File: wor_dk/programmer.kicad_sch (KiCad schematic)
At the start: 44 parts, among them J501 Prog_Ext, J502 USB_C_Receptacle_USB2.0_14P, J503 Prog, Q501 BSS84, SW501 SW_Push, U501 TLV1117-33, U502 LPC11U35FHI33_501, Y501 Crystal

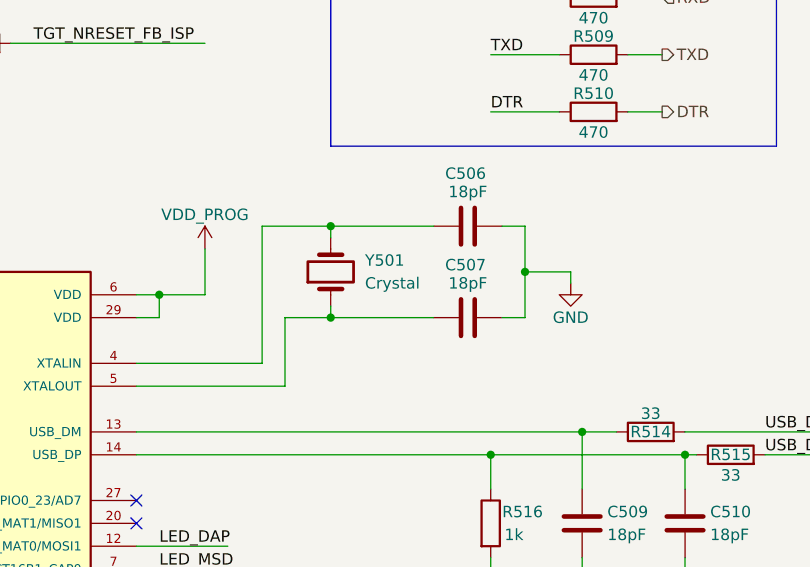
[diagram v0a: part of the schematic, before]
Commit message: wor_dk: add footprints & part info for transistor & ICs
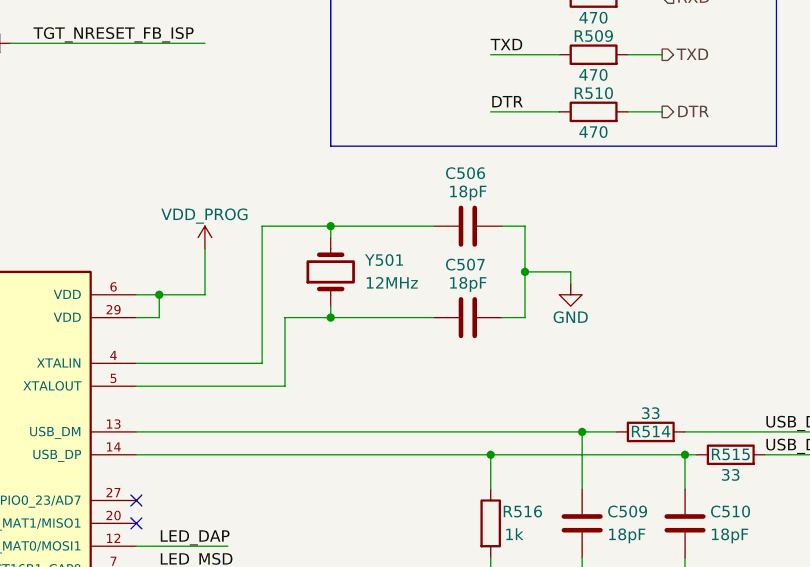
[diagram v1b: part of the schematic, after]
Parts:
- Q501: LCSC (none) -> C493579; MPN (none) -> BSS84,215; Manufacturer (none) -> Nexperia
- U501: footprint (none) -> Package_TO_SOT_SMD:SOT-223; LCSC (none) -> C37359; MPN (none) -> TLV1117-33IDCYR; Manufacturer (none) -> Texas Instruments
- Y501: value Crystal -> 12MHz
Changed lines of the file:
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@@
 			)
 		)
-		(property "Value" "Crystal"
+		(property "Value" "12MHz"
 			(at 224.79 88.8999 90)
 			(effects
@@
 			)
 		)
-		(property "Footprint" ""
+		(property "Footprint" "Package_TO_SOT_SMD:SOT-223"
 			(at 123.19 26.67 0)
 			(effects
@@
 			)
 		)
+		(property "LCSC" "C37359"
+			(at 123.19 26.67 0)
+			(effects
+				(font
+					(size 1.27 1.27)
+				)
+				(hide yes)
+			)
+		)
+		(property "MPN" "TLV1117-33IDCYR"
+			(at 123.19 26.67 0)
+			(effects
+				(font
+					(size 1.27 1.27)
+				)
+				(hide yes)
+			)
+		)
+		(property "Manufacturer" "Texas Instruments"
+			(at 123.19 26.67 0)
+			(effects
+				(font
+					(size 1.27 1.27)
+				)
+				(hide yes)
+			)
+		)
 		(pin "2"
 		)
@@
 			(at 236.22 125.73 0)
 			(effects
+				(font
+					(size 1.27 1.27)
+				)
+				(hide yes)
+			)
+		)
+		(property "LCSC" "C493579"
+			(at 236.22 125.73 0)
+			(effects
+				(font
+					(size 1.27 1.27)
+				)
+				(hide yes)
+			)
+		)
+		(property "MPN" "BSS84,215"
+			(at 236.22 125.73 0)
+			(effects
+				(font
+					(size 1.27 1.27)
+				)
+				(hide yes)
+			)
+		)
+		(property "Manufacturer" "Nexperia"
+			(at 236.22 125.73 0)
+			(effects

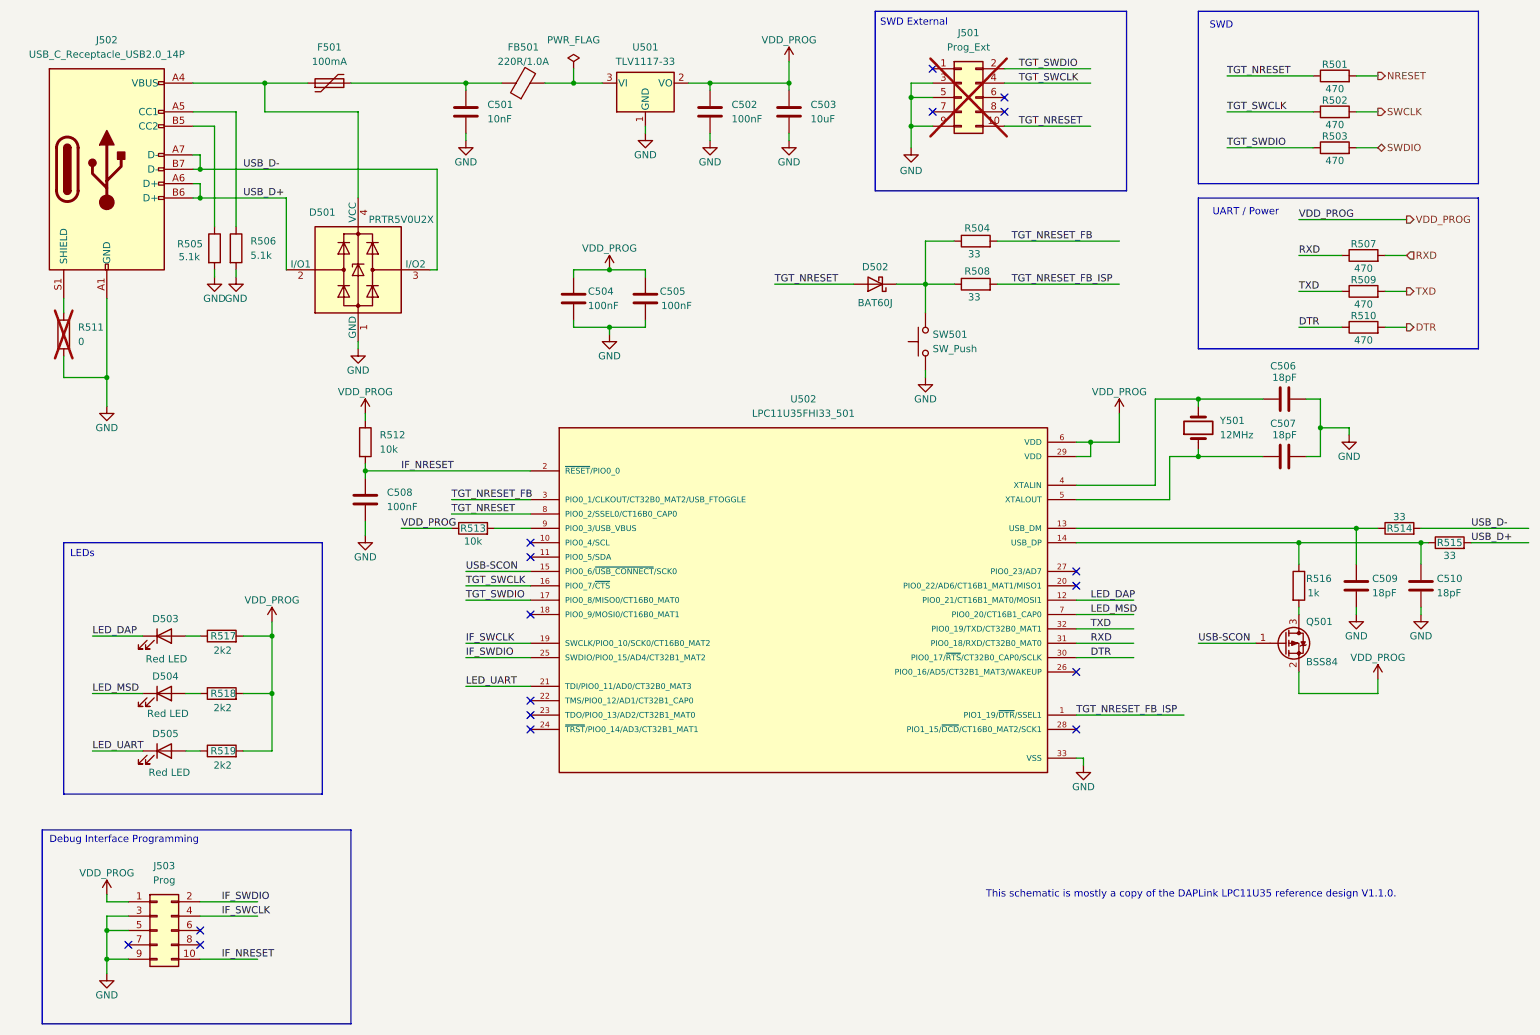
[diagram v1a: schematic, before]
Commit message: wor_dk: add all footprints & part info for connectors
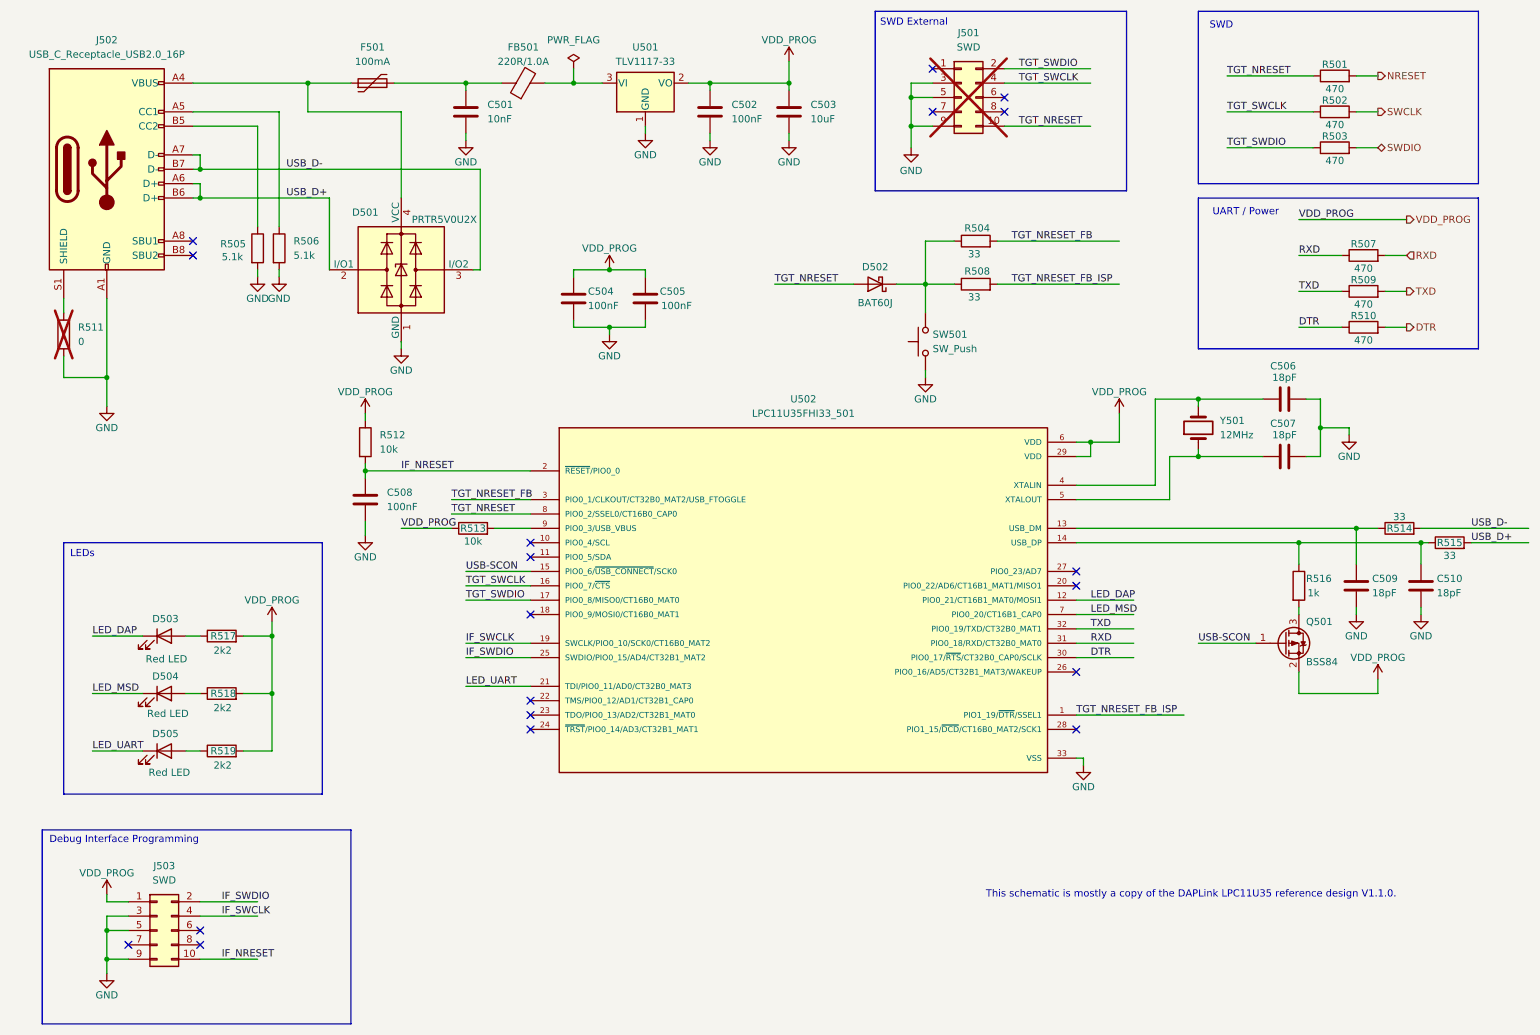
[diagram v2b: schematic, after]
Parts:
- removed J502: USB_C_Receptacle_USB2.0_14P, symbol Connector:USB_C_Receptacle_USB2.0_14P
- added J502: USB_C_Receptacle_USB2.0_16P, Connector_USB:USB_C_Receptacle_GCT_USB4105-xx-A_16P_TopMnt_Horizontal, symbol Connector:USB_C_Receptacle_USB2.0_16P
- J501: value Prog_Ext -> SWD; Comment (none) -> Connector for debugging / flashing external device; LCSC (none) -> C598540; MPN (none) -> 20021121-00010T4LF; Manufacturer (none) -> Amphenol ICC
- J503: value Prog -> SWD; Comment (none) -> Connector for debugging / flashing LCP11U35; LCSC (none) -> C598540; MPN (none) -> 20021121-00010T4LF; Manufacturer (none) -> Amphenol ICC
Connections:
- net GND: now also J502.A1 (GND), J502.A12 (GND), J502.B1 (GND), J502.B12 (GND)
- net USB_D+: now also J502.A6 (D+), J502.B6 (D+)
- net USB_D-: now also J502.A7 (D-), J502.B7 (D-)
- net at R505.1: now also J502.B5 (CC2)
- net at D501.4 (VCC), F501.1: now also J502.A4 (VBUS), J502.A9 (VBUS), J502.B4 (VBUS), J502.B9 (VBUS)
- net at R506.1: now also J502.A5 (CC1)
- net at R511.1: now also J502.S1 (SHIELD)
- no-connect marks 17 -> 19
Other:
- moved on the sheet: D501, F501, R505, R506

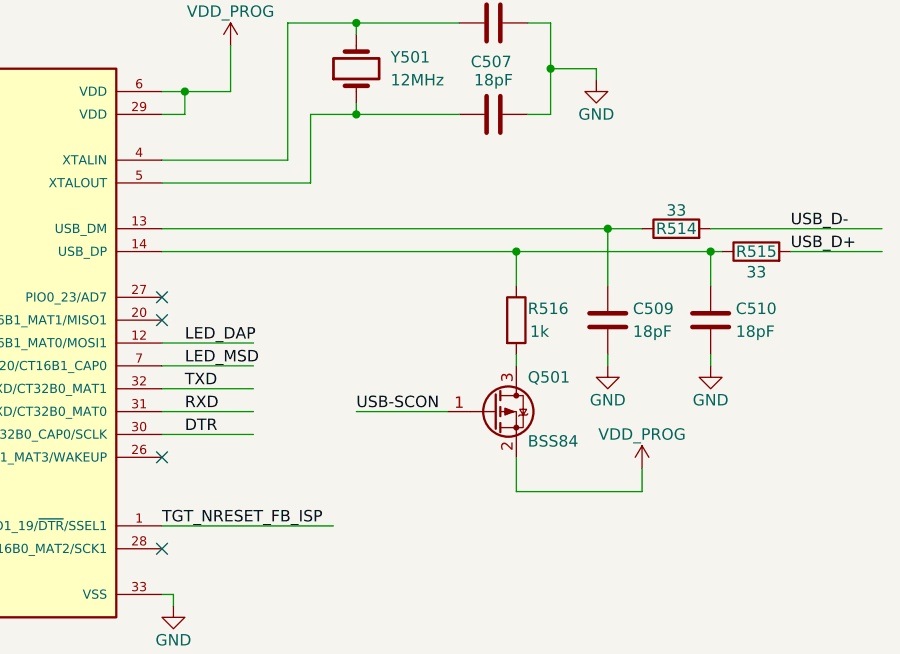
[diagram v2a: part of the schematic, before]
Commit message: wor_dk: add/modify USB data line filtering
- add filtering as suggested by FTDI application note AN232B-06
  section 6.2:
  "Some USB 2.0 hubs appear to be extremely sensitive to noise. A
  glitch on the USB lines can in some cases cause a device to hang.
  This problem can be fixed by adding two 47pF capacitors to ground on
  the USB DP and USB DM lines. These should be located between the 27W
  series resistors and the hub."
- using 33 Ω resistors and 33 pF capacitors instead of 27 Ω and 47 pF
  because parts with these values are already used
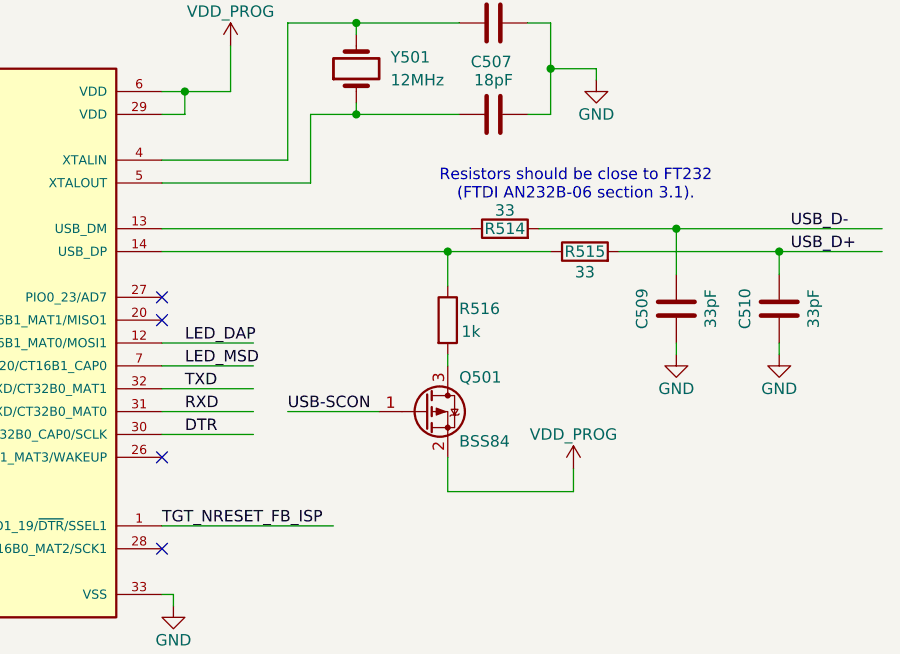
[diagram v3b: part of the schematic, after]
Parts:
- C509, C510: value 18pF -> 33pF; footprint Capacitor_SMD:C_0603_1608Metric -> Capacitor_SMD:C_0201_0603Metric; Comment JLCPCB basic part -> (none); LCSC C1647 -> C513616; MPN CL10C180JB8NNNC -> CC0201JRNPO8BN330; Manufacturer Samsung Electro-Mechanics -> YAGEO; Part Number (none) -> CC0201JRNPO8BN330
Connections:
- net USB_D+: now also C510.2
- net USB_D-: now also C509.2
- net at R515.1, R516.1, U502.14 (USB_DP): no longer C510.2
- net at R514.1, U502.13 (USB_DM): no longer C509.2
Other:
- note added: "Resistors should be close to FT232 (FTDI AN232B-06 section 3.1)."
- moved on the sheet: Q501, R514, R515, R516

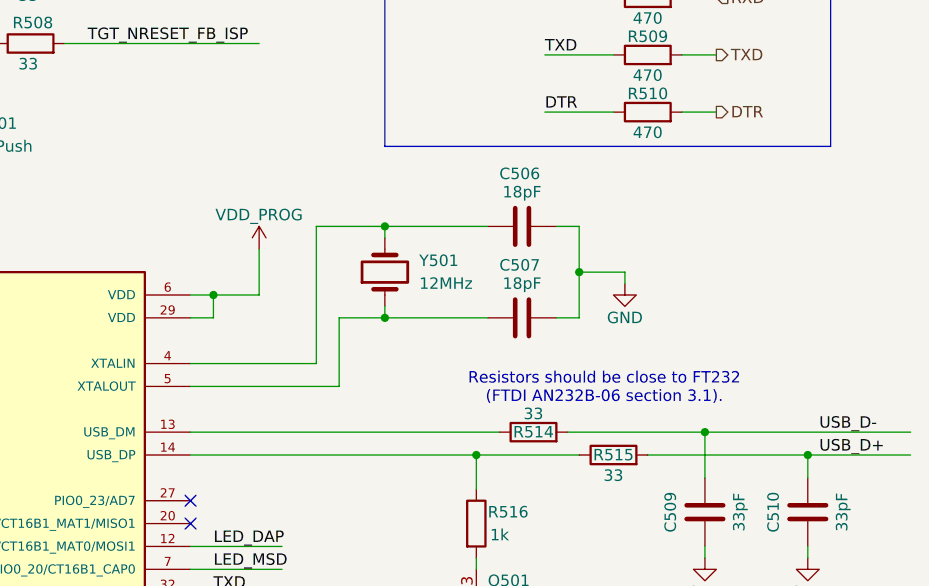
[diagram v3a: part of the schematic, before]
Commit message: wor_dk: add footprint & part info for 12 MHz crystal
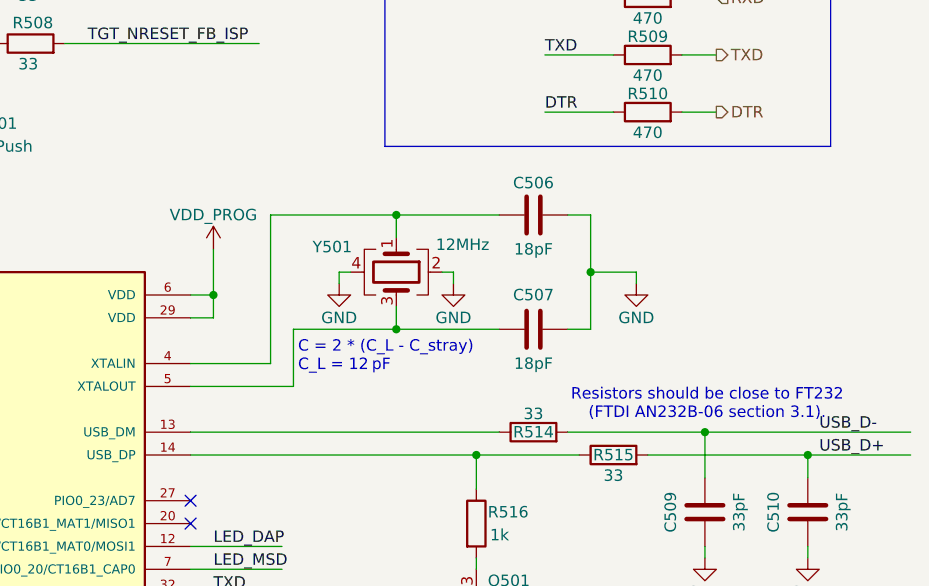
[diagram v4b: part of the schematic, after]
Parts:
- removed Y501: 12MHz, symbol Device:Crystal
- added Y501: 12MHz, Crystal:Crystal_SMD_SeikoEpson_TSX3225-4Pin_3.2x2.5mm, symbol Device:Crystal_GND24
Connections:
- net GND: now also Y501.2, Y501.4
- net at C507.1, U502.5 (XTALOUT): now also Y501.3
- net at C506.1, U502.4 (XTALIN): now also Y501.1
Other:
- note added: "C = 2 * (C_L - C_stray) C_L = 12 pF"
- moved on the sheet: C506, C507

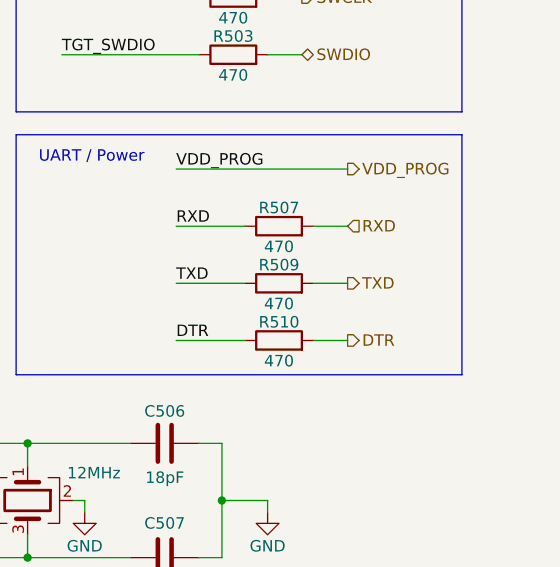
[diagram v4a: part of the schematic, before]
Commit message: wor_dk: schematic: fix LPC11U35 pins
The following signals of the LPC11U35 DAPLink were accidentally
connected due to identical labels on both sides:
- RXD across R507
- TXD across R509
- DTR across R510
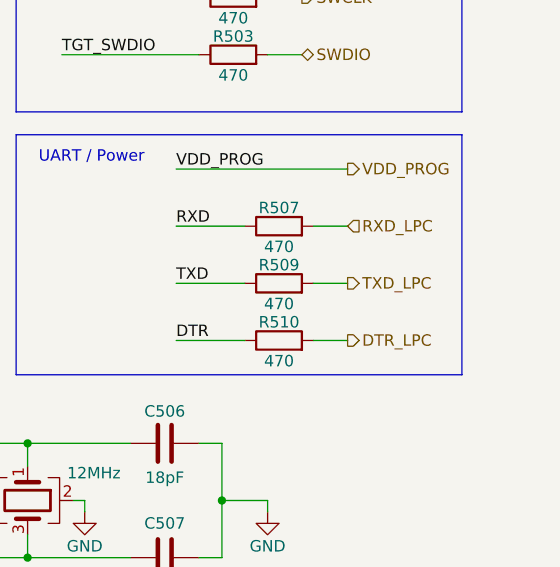
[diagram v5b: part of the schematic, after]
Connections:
- net DTR: no longer R510.2
- net RXD: no longer R507.2
- net TXD: no longer R509.2
- new net DTR_LPC: R510.2
- new net RXD_LPC: R507.2
- new net TXD_LPC: R509.2
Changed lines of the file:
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@@
 		)
 	)
-	(hierarchical_label "DTR"
+	(hierarchical_label "DTR_LPC"
 		(shape output)
 		(at 257.81 69.85 0)
@@
 		)
 	)
-	(hierarchical_label "TXD"
+	(hierarchical_label "TXD_LPC"
 		(shape output)
 		(at 257.81 63.5 0)
@@
 		)
 	)
-	(hierarchical_label "RXD"
+	(hierarchical_label "RXD_LPC"
 		(shape input)
 		(at 257.81 57.15 0)

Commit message: wor_dk: PCB: use KiCAD HVQFN-32 footprint instead of downloaded
This fixes all remaining DRC issues.
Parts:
- U502: footprint NXP:QFN50P500X500X85-33N -> Package_DFN_QFN:HVQFN-32-1EP_5x5mm_P0.5mm_EP3.1x3.1mm_ThermalVias
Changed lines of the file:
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@@
 			)
 		)
-		(property "Footprint" "NXP:QFN50P500X500X85-33N"
+		(property "Footprint" "Package_DFN_QFN:HVQFN-32-1EP_5x5mm_P0.5mm_EP3.1x3.1mm_ThermalVias"
 			(at 151.13 118.11 0)
 			(effects

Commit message: wor_dk: BOM: add JLCPCB part number for LPC11U35
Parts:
- U502: LCSC (none) -> C545247
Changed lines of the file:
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@@
+			)
+		)
+		(property "LCSC" "C545247"
+			(at 151.13 118.11 0)
+			(effects
+				(font
+					(size 1.27 1.27)
+				)
+				(hide yes)
 			)
 		)
